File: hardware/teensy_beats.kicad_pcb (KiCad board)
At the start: 2 copper layers, 86.4 x 110 mm, 143 parts, among them J1 Conn_01x02_Female, J2 AudioJack3_Ground, J3 Conn_01x04_Male, Q1 BSS138, Q2 BSS138, SW1 Rotary_Encoder_Switch, SW2 Rotary_Encoder_Switch, SW3 Rotary_Encoder_Switch, SW4 Rotary_Encoder_Switch, SW5 SW_Push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

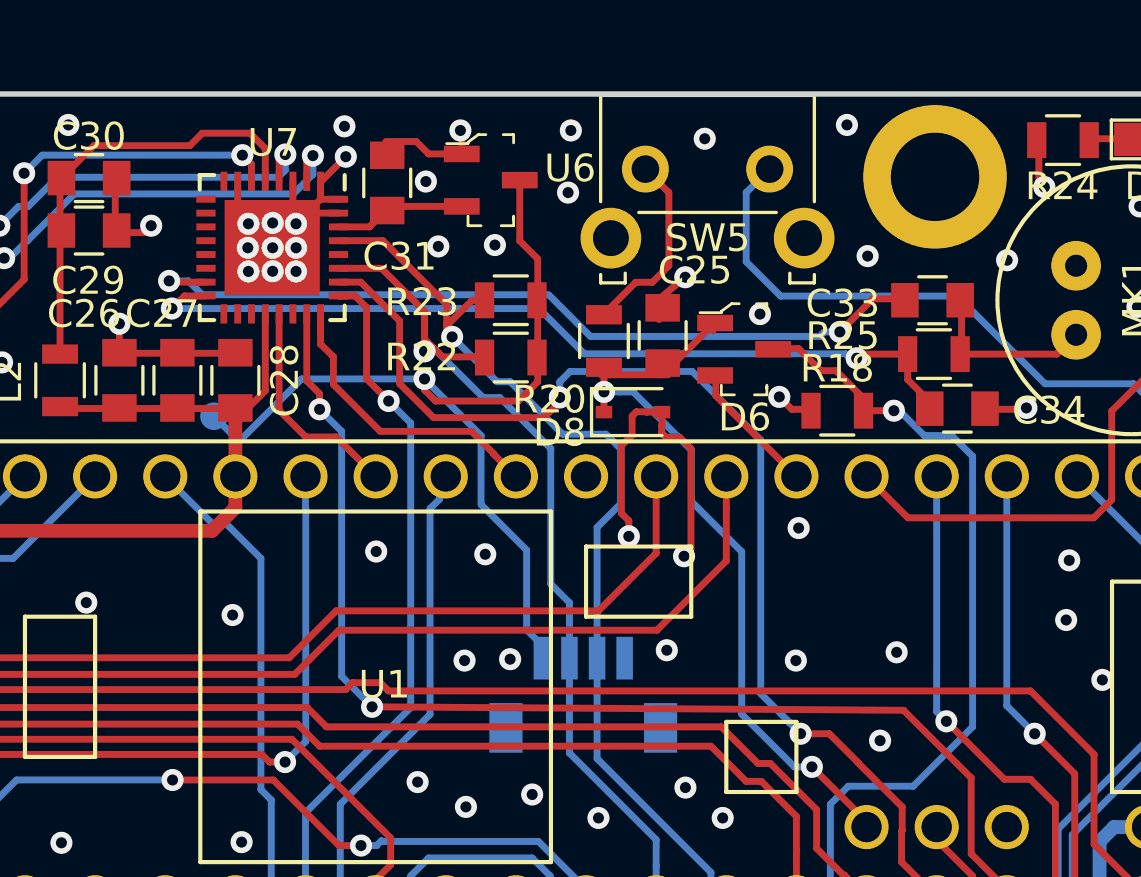
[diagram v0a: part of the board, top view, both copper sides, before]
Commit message: fixing incorrect PWR_BUTTON net on schematic and PCB
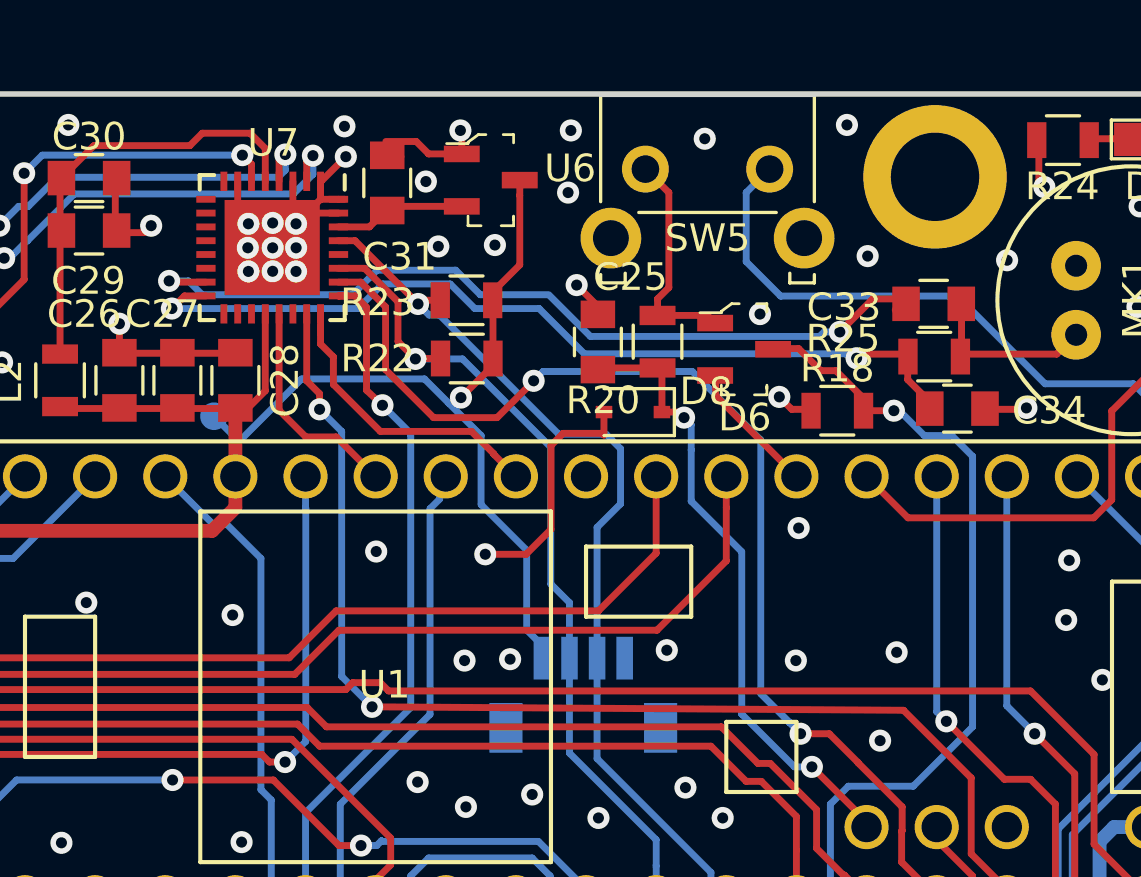
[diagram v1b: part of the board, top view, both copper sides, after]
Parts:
- D8: value D_Zener_Small -> Zener 3.3v
- moved C25 2.36 mm to (118.8, 46.3)
- moved R20 1.94 mm to (120.9, 46.2)
- moved R23 1.61 mm to (114.0, 44.8)
- moved R22 1.60 mm to (114.0, 46.9)
- moved C33 0.14 mm to (130.9, 44.9)
- moved R25 0.09 mm to (131.0, 46.8)
- turned D8 to 180 degrees
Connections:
- D6 pad 1: PWR_BTN -> Net-(D6-Pad1)
- R20 pad 1: Net-(R20-Pad1) -> Net-(D6-Pad1)
- SW5 pad 1: Net-(R20-Pad1) -> Net-(D6-Pad1)
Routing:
- net Net-(D6-Pad1): track 0.00 -> 8.55 mm
- net Net-(R20-Pad1): track 6.99 -> 0.00 mm
- net PWR_BTN: track 28.0 -> 22.8 mm
- net GND: track 153.9 -> 150.4 mm, vias 274 -> 272
- net +3V3: track 145.3 -> 142.0 mm
- net SCL: track 34.3 -> 32.7 mm
- net SDA: track 31.5 -> 30.0 mm
- net Net-(C34-Pad1): track 31.3 -> 32.0 mm
- net Net-(C33-Pad1): track 30.2 -> 30.9 mm

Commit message: changed pin mapping to add pg signal, added enable jumper for development. adding updated gerbers.
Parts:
- added J4: Conn_01x02_Male, Pin_Headers:Pin_Header_Straight_1x02_Pitch1.27mm, F.Cu at (122.1, 43.2)
- moved C36 0.47 mm to (124.3, 69.1)
- turned R30 to 0 degrees
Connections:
- U1 pad 10: Net-(U1-Pad10) -> E3B
- U1 pad 12: E3B -> TFT_DC
- U1 pad 47: TFT_DC -> PG
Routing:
- net GND: track 150.4 -> 185.9 mm, vias 272 -> 285
- net PG: track 2.24 -> 16.9 mm
- net TFT_DC: track 75.4 -> 68.3 mm, vias 1 -> 2
- net Net-(D6-Pad3): track 61.1 -> 66.3 mm
- net E3B: track 49.8 -> 54.0 mm, vias 1 -> 2
- net VBUS: track 51.2 -> 49.2 mm
- net LRCLK: track 42.8 -> 44.0 mm
- net BATT_STAT2: track 26.6 -> 25.4 mm
- net Net-(R30-Pad1): track 2.38 -> 3.36 mm
- net +BATT: track 110.4 -> 111.2 mm
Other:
- board text added: "Teensy Beats Shield 0.9.1"
- board text removed: "Teensy Beats Shield 0.9.0"
